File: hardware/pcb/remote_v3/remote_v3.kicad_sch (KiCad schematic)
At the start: 26 parts

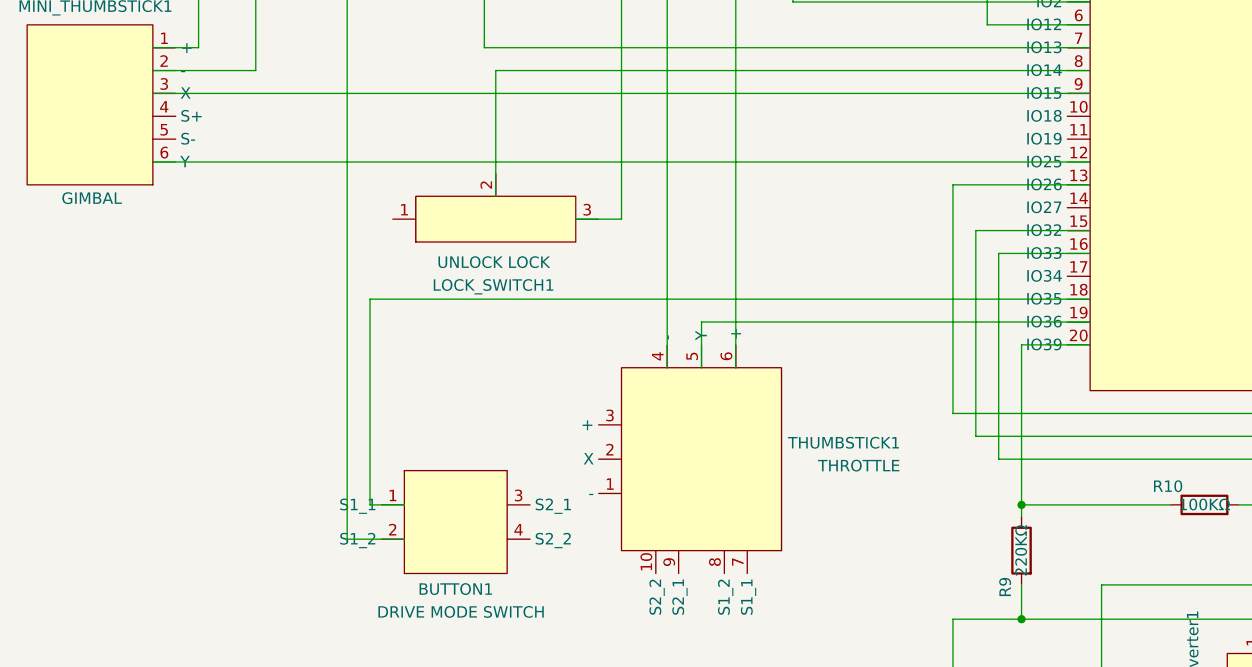
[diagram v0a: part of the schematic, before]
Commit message: remote: Update PCB for remote.
Fix the issue that GPIO 35 does not have internal PULLUP resistor.
So switch the pin with the gimbal thumbstick input Y, instead of the
drive mode button.

Update sensor and tag pcb as well to reflect the changes.
- tag: Use pin 39 for battery measurement and revert the resistor value
  change that's done in the previous commit.
- sensor: Fix a wiring issue.
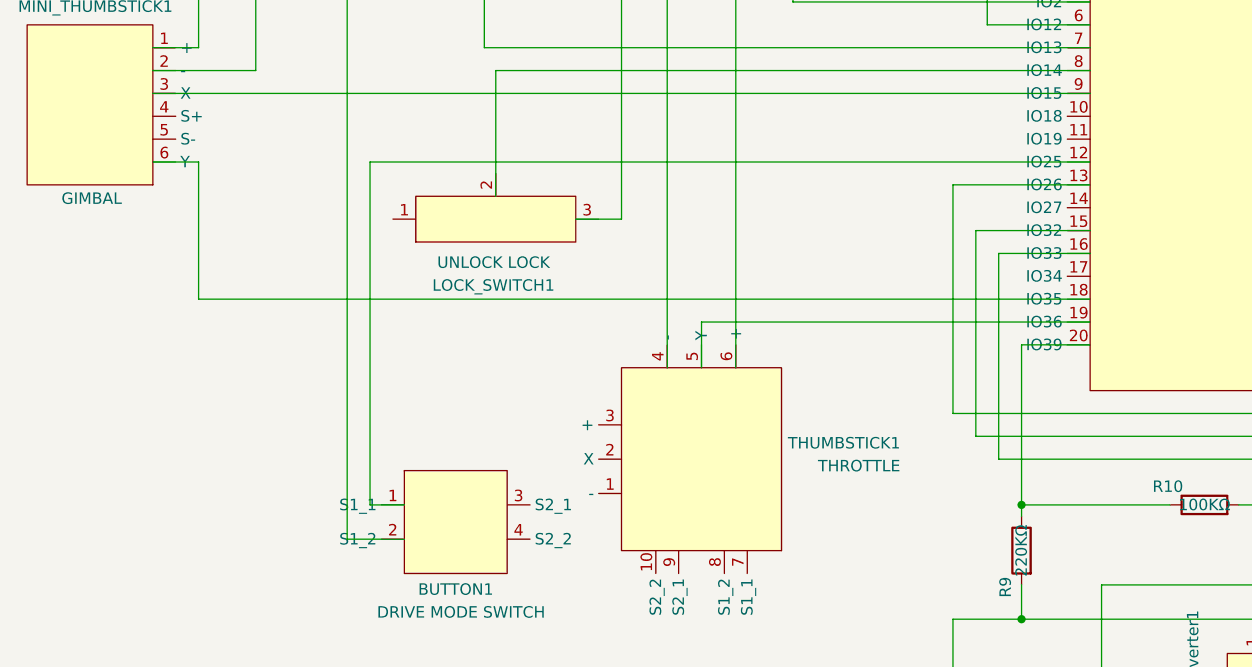
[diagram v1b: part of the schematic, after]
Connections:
- net at MINI_THUMBSTICK1.6 (Y): now also ESP32_UWB1.18 (IO35); no longer ESP32_UWB1.12 (IO25)
- net at BUTTON1.1 (S1_1): now also ESP32_UWB1.12 (IO25); no longer ESP32_UWB1.18 (IO35)
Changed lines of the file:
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@@
 	(title_block
 		(title "Autocam Remote")
-		(date "2025-03-18")
-		(rev "v0.5")
+		(date "2025-03-27")
+		(rev "v0.6")
 	)
 	(junction
@@
 	(wire
 		(pts
+			(xy 39.37 115.57) (xy 138.43 115.57)
+		)
+		(stroke
+			(width 0)
+			(type default)
+		)
+	)
+	(wire
+		(pts
 			(xy 67.31 80.01) (xy 86.36 80.01)
 		)
@@
 	(wire
 		(pts
-			(xy 58.42 115.57) (xy 58.42 138.43)
-		)
-		(stroke
-			(width 0)
-			(type default)
-		)
-	)
-	(wire
-		(pts
 			(xy 213.36 104.14) (xy 195.58 104.14)
 		)
@@
 	(wire
 		(pts
+			(xy 58.42 100.33) (xy 58.42 138.43)
+		)
+		(stroke
+			(width 0)
+			(type default)
+		)
+	)
+	(wire
+		(pts
 			(xy 135.89 58.42) (xy 135.89 72.39)
 		)
@@
 	(wire
 		(pts
-			(xy 138.43 115.57) (xy 58.42 115.57)
-		)
-		(stroke
-			(width 0)
-			(type default)
-		)
-	)
-	(wire
-		(pts
 			(xy 91.44 80.01) (xy 91.44 123.19)
 		)
@@
 	(wire
 		(pts
-			(xy 34.29 100.33) (xy 138.43 100.33)
-		)
-		(stroke
-			(width 0)
-			(type default)
-		)
-	)
-	(wire
-		(pts
 			(xy 181.61 74.93) (xy 163.83 74.93)
 		)
@@
 	(wire
 		(pts
+			(xy 138.43 100.33) (xy 58.42 100.33)
+		)
+		(stroke
+			(width 0)
+			(type default)
+		)
+	)
+	(wire
+		(pts
 			(xy 176.53 130.81) (xy 193.04 130.81)
 		)
@@
 	(wire
 		(pts
+			(xy 39.37 100.33) (xy 39.37 115.57)
+		)
+		(stroke
+			(width 0)
+			(type default)
+		)
+	)
+	(wire
+		(pts
 			(xy 67.31 33.02) (xy 67.31 80.01)
 		)
@@
 		)
 		(stroke
+			(width 0)
+			(type default)
+		)
+	)
+	(wire
+		(pts
+			(xy 34.29 100.33) (xy 39.37 100.33)
+		)
+		(stroke
